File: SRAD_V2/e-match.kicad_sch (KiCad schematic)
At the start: 27 parts, among them IC1 NCV81071BZR2G, IC2 NCV81071BZR2G, J2 691210910002, J3 691210910002, J4 691210910002, J5 691210910002, M1 FDC8878, Q1 AOSP36326C, Q2 AOSP36326C, Q3 AOSP36326C, Q4 AOSP36326C, Q6 FDS6630A, U3 TMCS1108A2UQDR

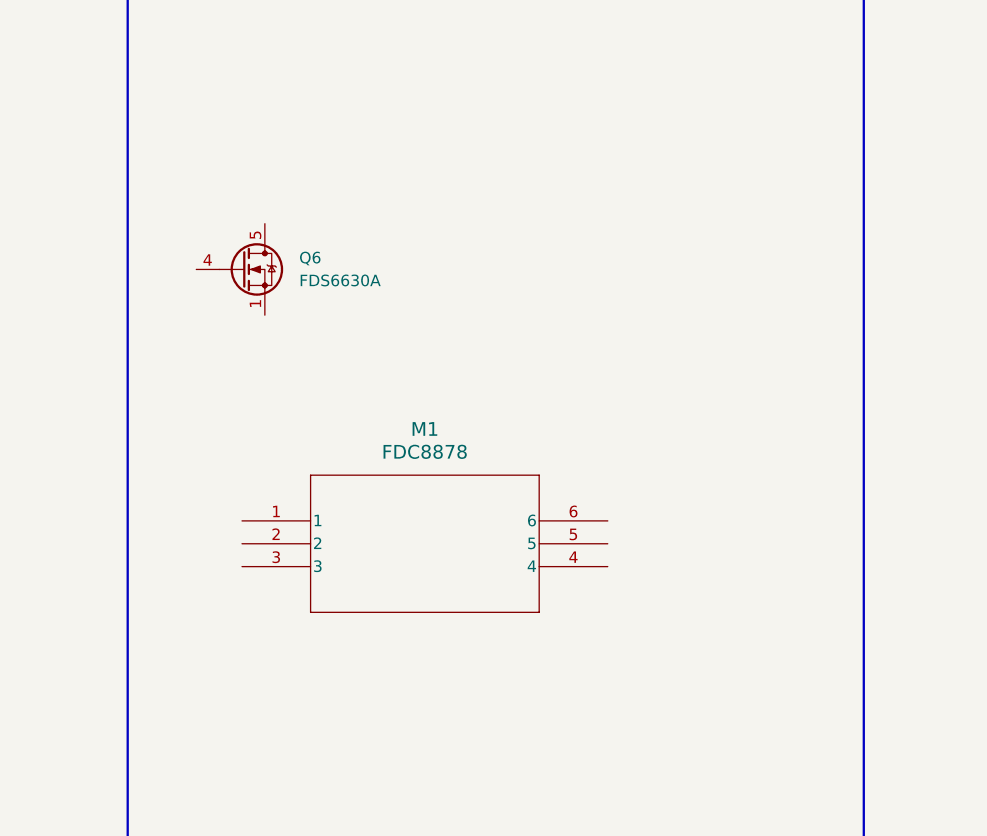
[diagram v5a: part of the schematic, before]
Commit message: added text-box for communication protocols in the schematic
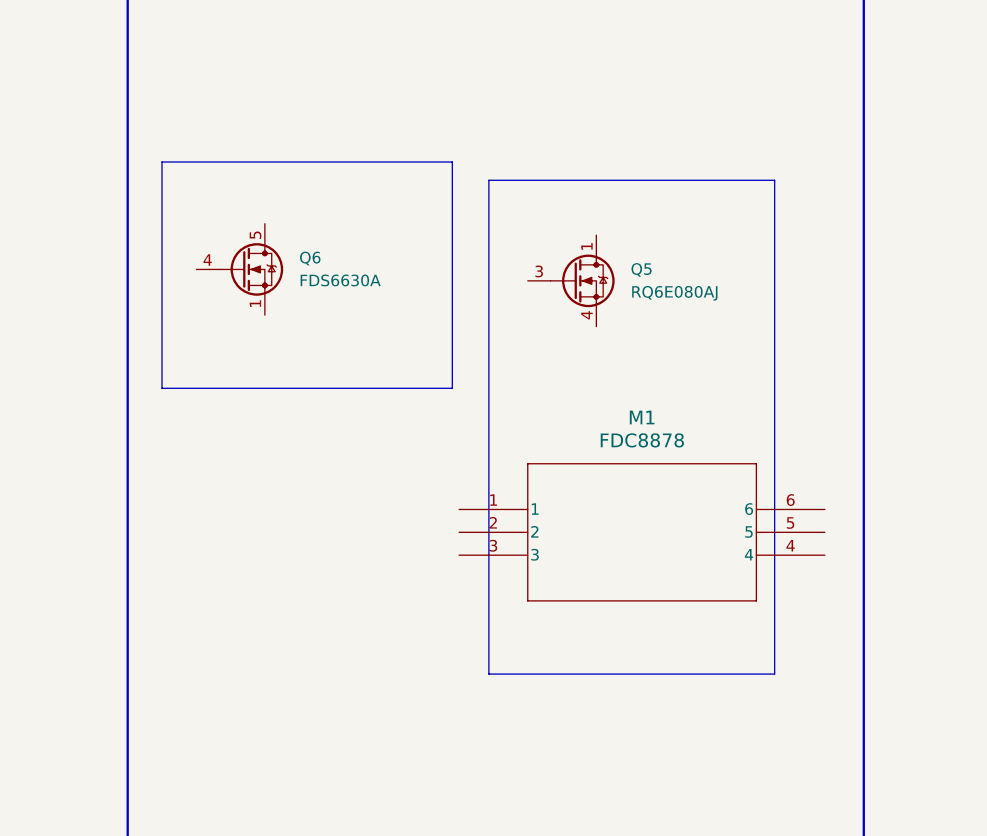
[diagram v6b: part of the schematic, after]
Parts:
- added Q5: RQ6E080AJ, Package_TO_SOT_SMD:SOT-23-6, symbol Transistor_FET:RQ6E080AJ
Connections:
- new net: Q5.1 (D), Q5.2 (D), Q5.5 (D), Q5.6 (D)
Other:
- moved on the sheet: M1
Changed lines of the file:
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@@
+	)
+	(rectangle
+		(start 125.73 84.582)
+		(end 157.988 109.728)
+		(stroke
+			(width 0)
+			(type default)
+		)
+		(fill
+			(type none)
+		)
 	)
 	(rectangle
@@
 			(width 0.254)
 			(type solid)
+		)
+		(fill
+			(type none)
+		)
+	)
+	(rectangle
+		(start 162.052 86.614)
+		(end 193.802 141.478)
+		(stroke
+			(width 0)
+			(type default)
 		)
 		(fill
@@
 				(path "/016ea6e5-09c6-43d4-b6cc-3404e2d65458/a2059f4c-c92f-483b-9b86-061767cb943d"
 					(reference "R6")
+					(unit 1)
+				)
+			)
+		)
+	)
+	(symbol
+		(lib_id "Transistor_FET:RQ6E080AJ")
+		(at 171.45 97.79 0)
+		(unit 1)
+		(exclude_from_sim no)
+		(in_bom yes)
+		(on_board yes)
+		(dnp no)
+		(fields_autoplaced yes)
+		(property "Reference" "Q5"
+			(at 177.8 96.5199 0)
+			(effects
+				(font
+					(size 1.27 1.27)
+				)
+				(justify left)
+			)
+		)
+		(property "Value" "RQ6E080AJ"
+			(at 177.8 99.0599 0)
+			(effects
+				(font
+					(size 1.27 1.27)
+				)
+				(justify left)
+			)
+		)
+		(property "Footprint" "Package_TO_SOT_SMD:SOT-23-6"
+			(at 176.53 99.695 0)
+			(effects
+				(font
+					(size 1.27 1.27)
+					(italic yes)
+				)
+				(justify left)
+				(hide yes)
+			)
+		)
+		(property "Datasheet" "https://fscdn.rohm.com/en/products/databook/datasheet/discrete/transistor/mosfet/rq6e080ajtcr-e.pdf"
+			(at 176.53 101.6 0)
+			(effects
+				(font
+					(size 1.27 1.27)
+				)
+				(justify left)
+				(hide yes)
+			)
+		)
+		(property "Description" "8A Id, 30V Vds, 16.5 mOhm RdsOn, N-Channel Small-Signal MOSFET, TSOT-23-6"
+			(at 171.45 97.79 0)
+			(effects
+				(font
+					(size 1.27 1.27)
+				)
+				(hide yes)
+			)
+		)
+		(pin "5"
+		)
+		(pin "3"
+		)
+		(pin "2"
+		)
+		(pin "1"
+		)
+		(pin "6"
+		)
+		(pin "4"
+		)
+		(instances
+			(project ""
+				(path "/016ea6e5-09c6-43d4-b6cc-3404e2d65458/a2059f4c-c92f-483b-9b86-061767cb943d"
+					(reference "Q5")
 					(unit 1)
 				)
@@
 	(symbol
 		(lib_id "FDC8878:FDC8878")
-		(at 134.62 124.46 0)
+		(at 158.75 123.19 0)
 		(unit 1)
 		(exclude_from_sim no)
@@
 		(fields_autoplaced yes)
 		(property "Reference" "M1"
-			(at 154.94 114.3 0)
+			(at 179.07 113.03 0)
 			(effects
 				(font
@@
 		)
 		(property "Value" "FDC8878"
-			(at 154.94 116.84 0)
+			(at 179.07 115.57 0)
 			(effects
 				(font
@@
 		)
 		(property "Footprint" "SuperSot6_SOT-23-6_1P6X2P9_ONS"
-			(at 134.62 124.46 0)
+			(at 158.75 123.19 0)
 			(effects
 				(font
@@
 		)
 		(property "Datasheet" "FDC8878"
-			(at 134.62 124.46 0)
+			(at 158.75 123.19 0)
 			(effects
 				(font
@@
 		)
 		(property "Description" ""
-			(at 134.62 124.46 0)
-			(effects
-				(font
+			(at 158.75 123.19 0)
+			(effects
+				(font

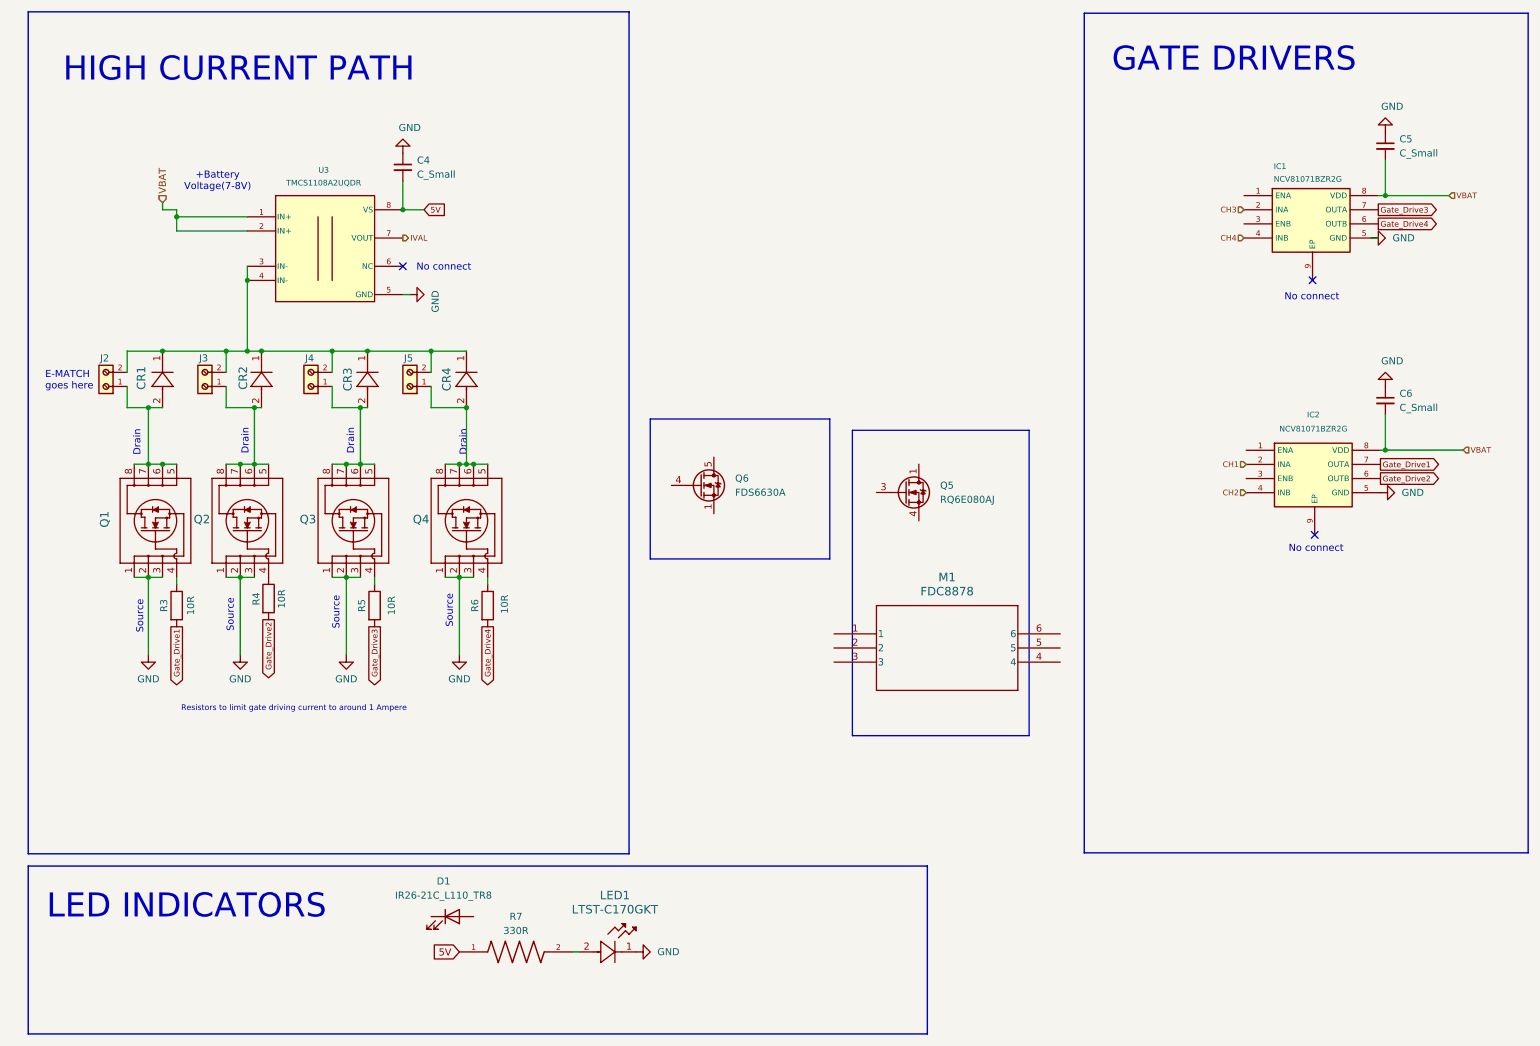
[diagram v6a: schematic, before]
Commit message: added bunch of decoupling capacitors, updated mosfet symbols with KICAD in-built ones etc
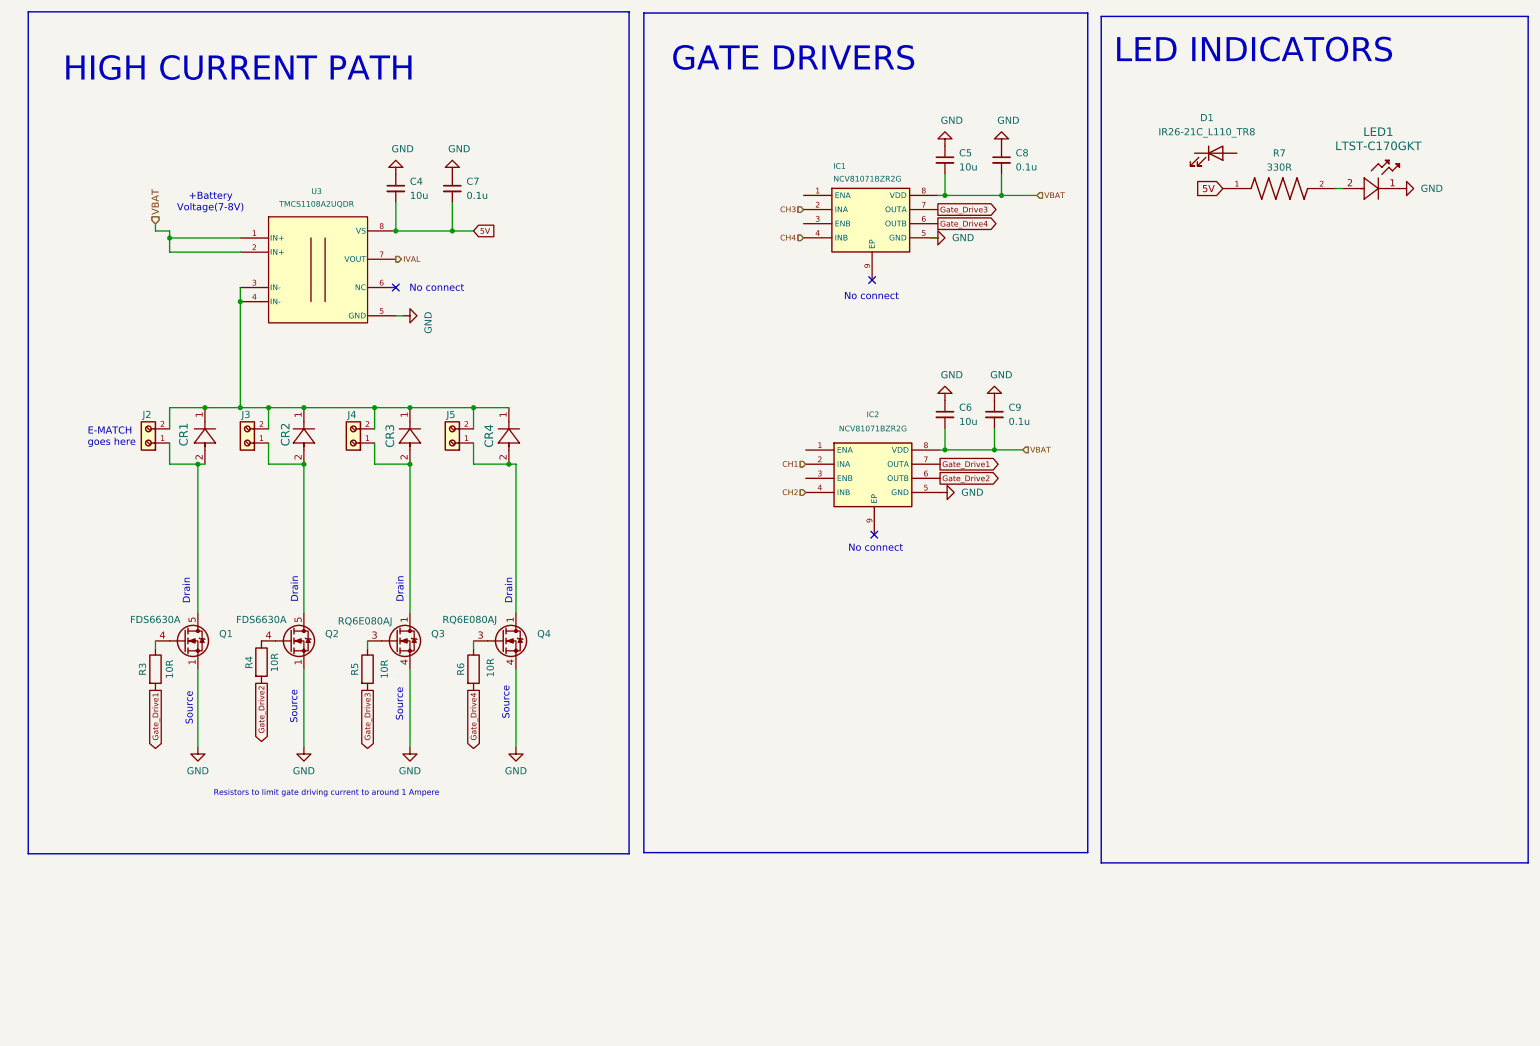
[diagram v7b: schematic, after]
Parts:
- removed M1: FDC8878, SuperSot6_SOT-23-6_1P6X2P9_ONS, symbol FDC8878:FDC8878
- removed Q1, Q2, Q3, Q4: AOSP36326C, SO8SOP-8L_AOS, symbol N-Ch Mosfet:AOSP36326C
- removed Q5: RQ6E080AJ, Package_TO_SOT_SMD:SOT-23-6, symbol Transistor_FET:RQ6E080AJ
- removed Q6: FDS6630A, Package_SO:SOIC-8_3.9x4.9mm_P1.27mm, symbol Transistor_FET:FDS6630A
- added C7, C8, C9: 0.1u, Capacitor_SMD:C_0603_1608Metric, symbol Device:C_Small
- added Q1, Q2: FDS6630A, Package_SO:SOIC-8_3.9x4.9mm_P1.27mm, symbol Transistor_FET:FDS6630A
- added Q3, Q4: RQ6E080AJ, Package_TO_SOT_SMD:SOT-23-6, symbol Transistor_FET:RQ6E080AJ
- C4, C5, C6: value C_Small -> 10u
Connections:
- net 5V: now also C7.2
- net GND: now also C7.1, C8.1, C9.1, Q1.1 (S), Q1.2 (S), Q1.3 (S), Q2.1 (S), Q2.2 (S), Q2.3 (S), Q3.4 (S), Q4.4 (S)
- net VBAT: now also C8.2, C9.2
- net at R6.1: now also Q4.3 (G)
- net at CR2.2, J3.1: now also Q2.5 (D), Q2.6 (D), Q2.7 (D), Q2.8 (D)
- net at R5.1: now also Q3.3 (G)
- net at CR3.2, J4.1: now also Q3.1 (D), Q3.2 (D), Q3.5 (D), Q3.6 (D)
- net at CR4.2, J5.1: now also Q4.1 (D), Q4.2 (D), Q4.5 (D), Q4.6 (D)
- net at CR1.2, J2.1: now also Q1.5 (D), Q1.6 (D), Q1.7 (D), Q1.8 (D)
- net at R3.1: now also Q1.4 (G)
- net at R4.1: now also Q2.4 (G)
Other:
- moved on the sheet: C4, C5, C6, CR1, CR2, CR3, CR4, D1, IC1, IC2, J2, J3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

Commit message: PDS routing
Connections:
- net 5V: now also C4.1, C7.1; no longer C4.2, C7.2
- net GND: now also C4.2, C5.2, C6.2, C7.2, C8.2, C9.2; no longer C4.1, C5.1, C6.1, C7.1, C8.1, C9.1
- net VBAT: now also C5.1, C6.1, C8.1, C9.1; no longer C5.2, C6.2, C8.2, C9.2
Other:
- moved on the sheet: C4, C5, C6, C7, C8, C9, D1, IC1, IC2, LED1, Q1, Q2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
